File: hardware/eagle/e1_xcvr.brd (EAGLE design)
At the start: 50 x 50 mm, 48 parts, among them T1 BC847C, U1 IDT82V2081, U3_2M 2.048 Mhz, U4_1M5 1.544 MHz, U6 TPS736XX

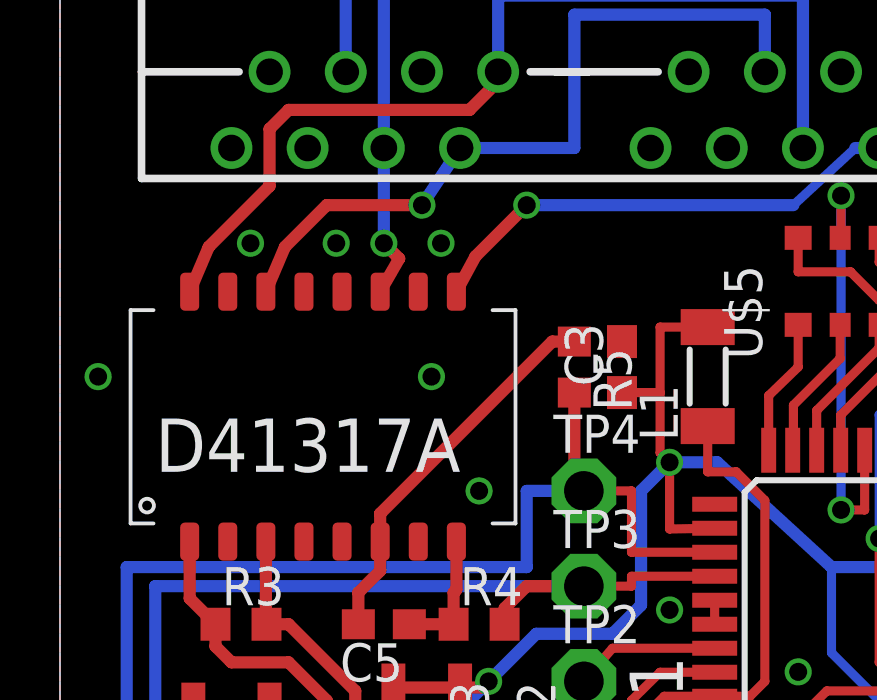
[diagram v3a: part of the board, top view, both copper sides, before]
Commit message: e1_xcvr.brd: minor routing improvement on TRING signal
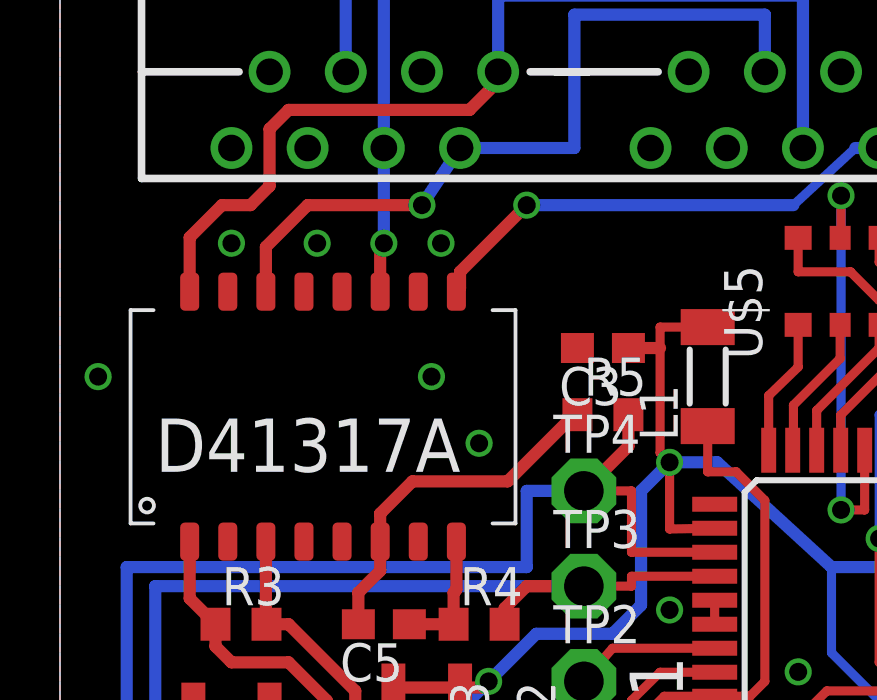
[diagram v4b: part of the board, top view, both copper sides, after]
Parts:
- moved R5 1.85 mm to (18.1, 24.1), turned to 0 degrees
- moved C3 0.90 mm to (18.1, 26.4), turned to 180 degrees
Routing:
- net N$31: track 12.8 -> 11.9 mm
- net N$34: track 32.8 -> 33.5 mm
- net N$40: track 25.6 -> 26.1 mm
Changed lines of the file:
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@@
 <element name="C1" library="rcl" package="C0603" value="100nF" x="37.1475" y="16.8275" rot="R270"/>
 <element name="C2" library="rcl" package="C0603" value="100nF" x="29.21" y="8.5725" rot="R270"/>
-<element name="C3" library="rcl" package="C0603" value="100nF" x="18.7325" y="25.7175" rot="R90"/>
+<element name="C3" library="rcl" package="C0603" value="100nF" x="18.0975" y="26.3525" rot="R180"/>
 <element name="C4" library="rcl" package="C0603" value="100nF" x="19.05" y="8.89" rot="R270"/>
 <element name="U$2" library="laforge" package="PULSE_BH" value="PULSE_T1094NL" x="8.5725" y="24.13" rot="R90"/>
@@
 <element name="D8" library="semicon-smd-ipc" package="SOD123" value="MBR0540T1" x="6.985" y="6.35" rot="R270"/>
 <element name="R4" library="rcl" package="R0603" value="0" x="13.97" y="17.145"/>
-<element name="R5" library="rcl" package="R0603" value="0" x="17.145" y="25.7175" rot="R270"/>
+<element name="R5" library="rcl" package="R0603" value="0" x="18.0975" y="24.13"/>
 <element name="C5" library="rcl" package="C0603" value="" x="10.795" y="17.145" rot="R180"/>
 <element name="L1" library="inductor-neosid" package="SM-1206" value="47nH" x="21.59" y="25.4" rot="R90">
@@
 <contactref element="U1" pad="44"/>
 <via x="24.60625" y="15.5575" extent="1-16" drill="0.6"/>
-<via x="9.2075" y="29.845" extent="1-16" drill="0.6"/>
+<via x="8.5725" y="29.845" extent="1-16" drill="0.6"/>
 <via x="12.7" y="29.845" extent="1-16" drill="0.6"/>
-<via x="6.35" y="29.845" extent="1-16" drill="0.6"/>
-<via x="13.97" y="21.59" extent="1-16" drill="0.6"/>
+<via x="5.715" y="29.845" extent="1-16" drill="0.6"/>
+<via x="13.97" y="23.1775" extent="1-16" drill="0.6"/>
 <via x="20.32" y="17.62125" extent="1-16" drill="0.6"/>
 <via x="31.27375" y="8.89" extent="1-16" drill="0.6"/>
@@
 <wire x1="35.8775" y1="30.48" x2="34.505" y2="30.48" width="0.3048" layer="1"/>
 <wire x1="34.505" y1="30.48" x2="34.505" y2="23.8125" width="0.3048" layer="1"/>
-<wire x1="18.7325" y1="24.8675" x2="20.0025" y2="24.8675" width="0.3048" layer="1"/>
-<wire x1="20.0025" y1="24.8675" x2="20.0025" y2="27.05" width="0.3048" layer="1"/>
 <wire x1="21.59" y1="27.05" x2="20.0025" y2="27.05" width="0.3048" layer="1"/>
 <via x="8.255" y="9.8425" extent="1-16" drill="0.6"/>
@@
 <wire x1="20.32" y1="20.32" x2="20.32" y2="22.5425" width="0.3048" layer="1"/>
 <wire x1="20.32" y1="22.5425" x2="20.0025" y2="22.86" width="0.3048" layer="1"/>
-<wire x1="20.0025" y1="22.86" x2="20.0025" y2="24.8675" width="0.3048" layer="1"/>
+<wire x1="20.0025" y1="22.86" x2="20.0025" y2="26.3525" width="0.3048" layer="1"/>
 <via x="20.32" y="22.5425" extent="1-16" drill="0.6"/>
+<wire x1="20.0025" y1="26.3525" x2="20.0025" y2="27.05" width="0.3048" layer="1"/>
 <wire x1="13.335" y1="15.035" x2="14.0825" y2="15.035" width="0.4064" layer="1"/>
 <wire x1="14.0825" y1="15.035" x2="14.2875" y2="15.24" width="0.4064" layer="1"/>
 <via x="14.2875" y="15.24" extent="1-16" drill="0.6"/>
 <wire x1="11.1125" y1="15.035" x2="13.335" y2="15.035" width="0.4064" layer="1"/>
+<wire x1="18.9475" y1="26.3525" x2="20.0025" y2="26.3525" width="0.4064" layer="1"/>
 </signal>
 <signal name="N$2">
@@
 <wire x1="15.5575" y1="19.05" x2="15.5575" y2="21.59" width="0.4064" layer="16"/>
 <wire x1="15.5575" y1="21.59" x2="17.4625" y2="21.59" width="0.4064" layer="16"/>
-<wire x1="17.145" y1="24.8675" x2="17.145" y2="21.9075" width="0.4064" layer="1"/>
-<wire x1="17.145" y1="21.9075" x2="17.4625" y2="21.59" width="0.4064" layer="1"/>
+<wire x1="18.9475" y1="24.13" x2="18.9475" y2="23.075" width="0.4064" layer="1"/>
+<wire x1="18.9475" y1="23.075" x2="17.4625" y2="21.59" width="0.4064" layer="1"/>
 </signal>
 <signal name="N$29">
@@
 <wire x1="9.945" y1="17.145" x2="9.945" y2="18.2" width="0.4064" layer="1"/>
 <wire x1="10.6725" y1="19.9" x2="10.6725" y2="20.8325" width="0.4064" layer="1"/>
-<wire x1="10.6725" y1="20.8325" x2="16.4075" y2="26.5675" width="0.4064" layer="1"/>
-<wire x1="17.145" y1="26.5675" x2="16.4075" y2="26.5675" width="0.4064" layer="1"/>
+<wire x1="17.2475" y1="24.13" x2="17.145" y2="24.13" width="0.4064" layer="1"/>
+<wire x1="17.145" y1="24.13" x2="14.9225" y2="21.9075" width="0.4064" layer="1"/>
+<wire x1="14.9225" y1="21.9075" x2="11.7475" y2="21.9075" width="0.4064" layer="1"/>
+<wire x1="11.7475" y1="21.9075" x2="10.6725" y2="20.8325" width="0.4064" layer="1"/>
 </signal>
 <signal name="N$40">
@@
 <wire x1="13.335" y1="33.02" x2="12.065" y2="31.115" width="0.4064" layer="16"/>
 <via x="12.065" y="31.115" extent="1-16" drill="0.6"/>
-<wire x1="12.065" y1="31.115" x2="8.89" y2="31.115" width="0.4064" layer="1"/>
-<wire x1="8.89" y1="31.115" x2="7.4975" y2="29.7225" width="0.4064" layer="1"/>
-<wire x1="6.8625" y1="28.23" x2="7.4975" y2="29.7225" width="0.4064" layer="1"/>
+<wire x1="12.065" y1="31.115" x2="8.255" y2="31.115" width="0.4064" layer="1"/>
+<wire x1="6.8625" y1="28.23" x2="6.8625" y2="29.7225" width="0.4064" layer="1"/>
+<wire x1="6.8625" y1="29.7225" x2="8.255" y2="31.115" width="0.4064" layer="1"/>
 </signal>
 <signal name="N$22">
@@
 <wire x1="7.62" y1="34.29" x2="6.985" y2="33.655" width="0.4064" layer="1"/>
 <wire x1="6.985" y1="33.655" x2="6.985" y2="31.75" width="0.4064" layer="1"/>
-<wire x1="6.985" y1="31.75" x2="4.9575" y2="29.7225" width="0.4064" layer="1"/>
-<wire x1="4.3225" y1="28.23" x2="4.9575" y2="29.7225" width="0.4064" layer="1"/>
+<wire x1="6.985" y1="31.75" x2="6.35" y2="31.115" width="0.4064" layer="1"/>
+<wire x1="6.35" y1="31.115" x2="5.3975" y2="31.115" width="0.4064" layer="1"/>
+<wire x1="5.3975" y1="31.115" x2="4.3225" y2="30.04" width="0.4064" layer="1"/>
+<wire x1="4.3225" y1="28.23" x2="4.3225" y2="30.04" width="0.4064" layer="1"/>
 </signal>
 <signal name="N$32">
@@
 <wire x1="26.51125" y1="33.02" x2="24.4475" y2="31.115" width="0.3048" layer="16"/>
 <wire x1="24.4475" y1="31.115" x2="15.5575" y2="31.115" width="0.4064" layer="16"/>
-<wire x1="15.5575" y1="31.115" x2="13.8475" y2="29.405" width="0.4064" layer="1"/>
-<wire x1="13.2125" y1="28.23" x2="13.8475" y2="29.405" width="0.4064" layer="1"/>
+<wire x1="15.5575" y1="31.115" x2="13.335" y2="28.8925" width="0.4064" layer="1"/>
+<wire x1="13.335" y1="28.8925" x2="13.335" y2="28.3525" width="0.4064" layer="1"/>
+<wire x1="13.335" y1="28.3525" x2="13.2125" y2="28.23" width="0.4064" layer="1"/>
 </signal>
 <signal name="N$36">
@@
 <wire x1="10.795" y1="33.02" x2="10.795" y2="29.845" width="0.4064" layer="16"/>
 <via x="10.795" y="29.845" extent="1-16" drill="0.6"/>
-<wire x1="10.6725" y1="28.23" x2="11.3075" y2="29.3325" width="0.4064" layer="1"/>
-<wire x1="11.3075" y1="29.3325" x2="10.795" y2="29.845" width="0.4064" layer="1"/>
+<wire x1="10.6725" y1="28.23" x2="10.6725" y2="29.7225" width="0.4064" layer="1"/>
+<wire x1="10.6725" y1="29.7225" x2="10.795" y2="29.845" width="0.4064" layer="1"/>
 </signal>
 <signal name="VIN" class="1">
